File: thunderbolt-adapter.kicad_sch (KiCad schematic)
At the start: 191 parts, among them J1 DX07S024JJ2R1300, J2 PCIe_x4_Conn_EdgeMount, U1 SI52112-B6-GT, U3 TPS65983BAZBHR, U4 JHL6340SLLSQ, U5 MX25L8006EM1I-12G, Y1 25MHz

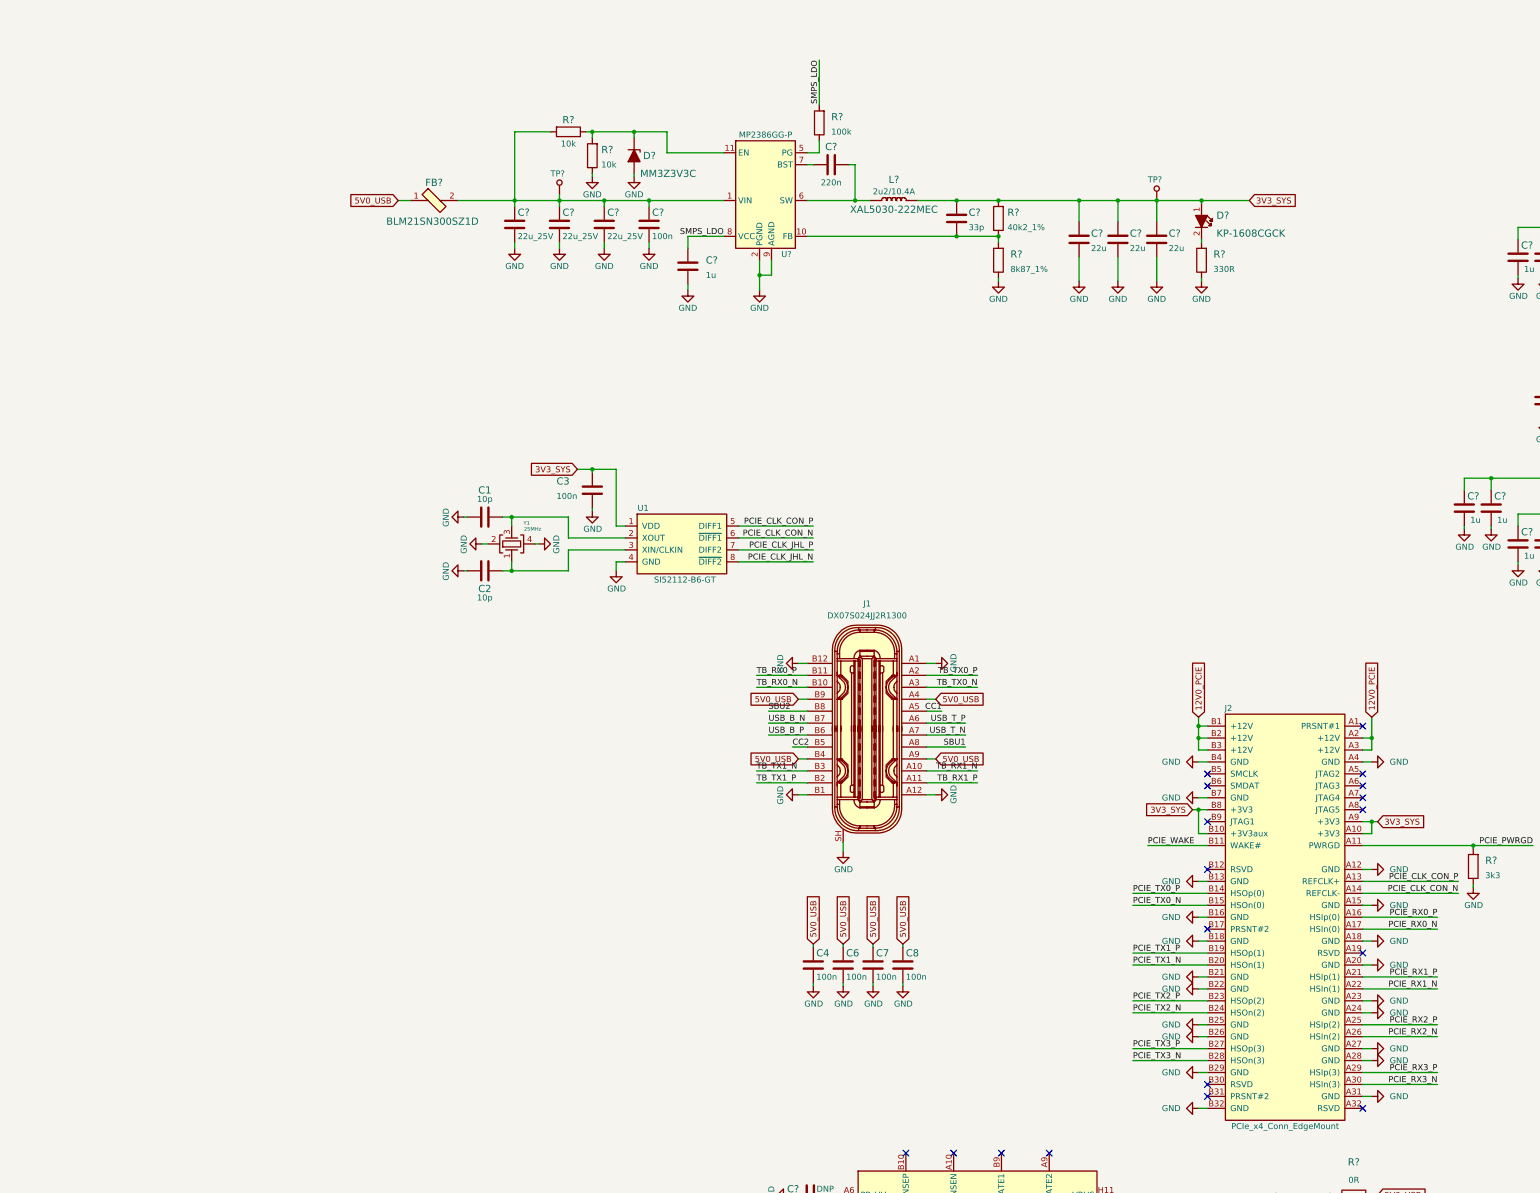
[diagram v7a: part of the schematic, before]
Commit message: Add 12V buck-boost converter
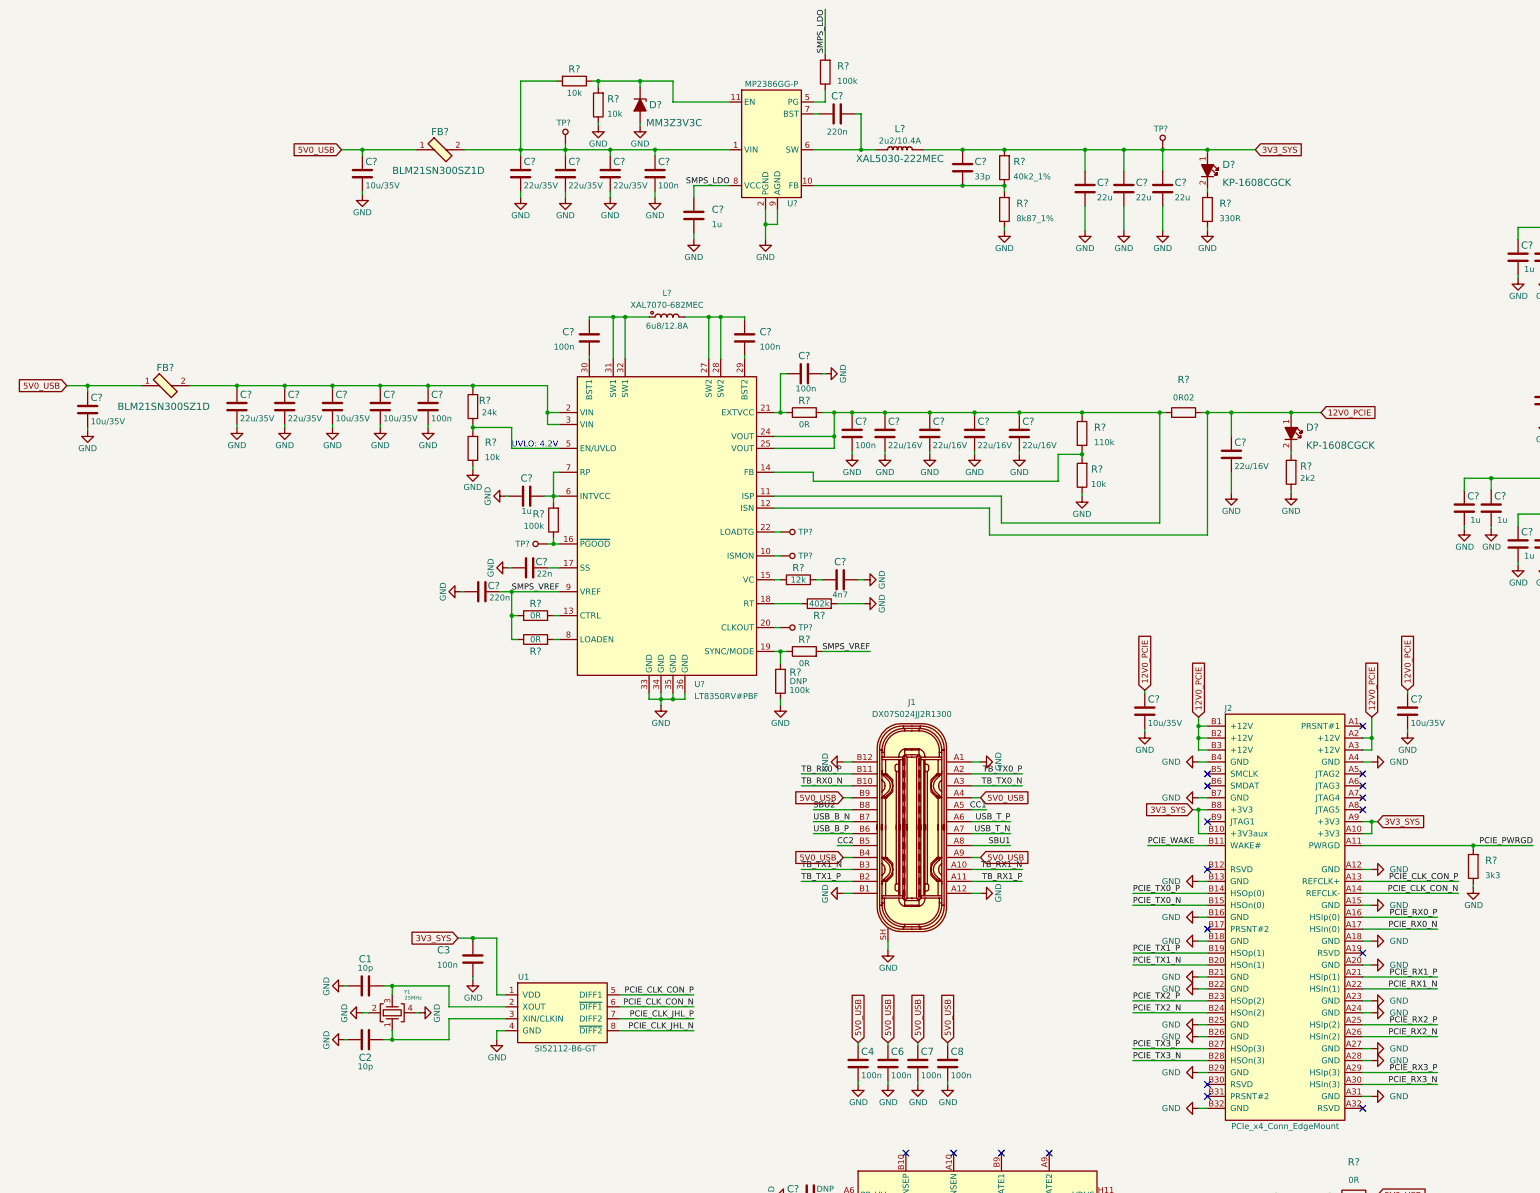
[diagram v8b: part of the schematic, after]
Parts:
- removed C? (x3): C_22u_0805_25V, antmicro-footprints:0805-cap, symbol antmicroCapacitorsmisc:C_22u_0805_25V
- added C? (x6): C_10u_0805_35V, antmicro-footprints:0805-cap, symbol antmicroCapacitorsmisc:C_10u_0805_35V
- added C? (x5): C_22u_0603_16V, antmicro-footprints:0603-cap, symbol antmicroCapacitors0603:C_22u_0603_16V
- added C?: C_1u_0402, antmicro-footprints:0402-cap, symbol antmicroCapacitors0402:C_1u_0402
- added C? (x5): C_22u_1206_35V, antmicro-footprints:1206-cap, symbol antmicroCapacitorsmisc:C_22u_1206_35V
- added C?: C_22n_0402, antmicro-footprints:0402-cap, symbol antmicroCapacitors0402:C_22n_0402
- added C? (x5): C_100n_0402, antmicro-footprints:0402-cap, symbol antmicroCapacitors0402:C_100n_0402
- added C?: C_4n7_0402, antmicro-footprints:0402-cap, symbol antmicroCapacitors0402:C_4n7_0402
- added C?: C_220n_0402, antmicro-footprints:0402-cap, symbol antmicroCapacitors0402:C_220n_0402
- added D?: KP-1608CGCK, antmicro-footprints:LED_0603, symbol antmicroLEDIndicationDiscrete:KP-1608CGCK
- added FB?: BLM21SN300SZ1D, antmicro-footprints:0805-res, symbol antmicroFerriteBeadsandChips:BLM21SN300SZ1D
- added L?: XAL7070-682MEC, antmicro-footprints:Coilcraft-XAL7070, symbol antmicroFixedInductors:XAL7070-682MEC
- added R? (x4): R_0R_0402, antmicro-footprints:0402-res, symbol antmicroResistors0402:R_0R_0402
- added R?: R_402k_0402, antmicro-footprints:0402-res, symbol antmicroResistors0402:R_402k_0402
- added R? (x2): R_10k_0402, antmicro-footprints:0402-res, symbol antmicroResistors0402:R_10k_0402
- added R?: R_0R02_1206, antmicro-footprints:1206-res, symbol antmicroResistorsmisc:R_0R02_1206
- added R?: R_12k_0402, antmicro-footprints:0402-res, symbol antmicroResistors0402:R_12k_0402
- added R? (x2): R_100k_0402, antmicro-footprints:0402-res, symbol antmicroResistors0402:R_100k_0402
- added R?: R_24k_0402, antmicro-footprints:0402-res, symbol antmicroResistors0402:R_24k_0402
- added R?: R_2k2_0402, antmicro-footprints:0402-res, symbol antmicroResistors0402:R_2k2_0402
- added R?: R_110k_0402, antmicro-footprints:0402-res, symbol antmicroResistors0402:R_110k_0402
- added TP? (x4): TP_SMD1MM, antmicro-footprints:Testpoint_smd_1mm, symbol antmicroTestPoints:TP_SMD1MM
- added U?: LT8350RV#PBF, antmicro-footprints:LT8350, symbol antmicroDCDCConverters:LT8350RV#PBF
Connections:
- net 12V0_PCIE: now also C?.1, C?.1, C?.2, D?.1, R?.2, U?.12 (ISN)
- net 5V0_USB: now also C?.1, C?.1, FB?.1
- net GND: now also C?.1, C?.1, C?.1, C?.1, C?.1, C?.1, C?.1, C?.2, C?.2, C?.2, C?.2, C?.2, C?.2, C?.2, C?.2, C?.2, C?.2, C?.2, C?.2, C?.2, C?.2, C?.2, C?.2, R?.1, R?.1, R?.1, R?.1, R?.2, U?.33 (GND), U?.34 (GND), U?.35 (GND), U?.36 (GND)
- net at C?.1, FB?.2, R?.2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: now also C?.1, C?.1, C?.1
- new net: R?.2, U?.8 (LOADEN)
- new net: C?.1, C?.2, C?.2, C?.2, C?.2, R?.1, R?.1, R?.2, U?.11 (ISP), U?.24 (VOUT), U?.25 (VOUT)
- new net: TP?.1, U?.10 (ISMON)
- new net: R?.1, U?.18 (RT)
- new net: R?.2, R?.2, U?.14 (FB)
- new net: C?.1, R?.2, U?.6 (INTVCC), U?.7 (RP)
- new net: R?.2, U?.13 (CTRL)
- new net: R?.1, U?.15 (VC)
- new net: R?.1, TP?.1, U?.16 (~{PGOOD})
- new net: C?.2, U?.17 (SS)
- new net: R?.1, R?.2, U?.19 (SYNC/MODE)
- new net: C?.1, C?.1, C?.1, C?.1, C?.1, FB?.2, R?.2, U?.2 (VIN), U?.3 (VIN)
- new net: TP?.1, U?.20 (CLKOUT)
- new net: C?.1, R?.1, U?.21 (EXTVCC)
- new net: TP?.1, U?.22 (LOADTG)
- new net: C?.2, L?.2 (P), U?.27 (SW2), U?.28 (SW2)
- new net: C?.1, U?.29 (BST2)
- new net: C?.1, U?.30 (BST1)
- new net: C?.2, L?.1 (P), U?.31 (SW1), U?.32 (SW1)
- new net: R?.1, R?.2, U?.5 (EN/UVLO)
- new net: D?.2, R?.2
- new net: C?.1, R?.2
- new net SMPS_VREF: C?.2, R?.1, R?.1, R?.2, U?.9 (VREF)
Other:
- note added: "UVLO: 4.2V"
- moved on the sheet: C1, C2, C3, C4, C6, C7, C8, C?, D?, FB?, J1, L?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
